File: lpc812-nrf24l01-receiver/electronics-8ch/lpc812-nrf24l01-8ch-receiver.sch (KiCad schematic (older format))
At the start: 23 parts, among them J1 CH1, J2 CH2/Rx, J3 CH3, J4 CH4, J5 CH5/Tx, J6 CH6, J7 CH7, J8 CH8, SW1 BIND/ISP, U1 MCP1703A-3302_SOT23, U2 LPC812M101JDH20, U3 NRF24L01_E01_ML01, Y1 12MHz

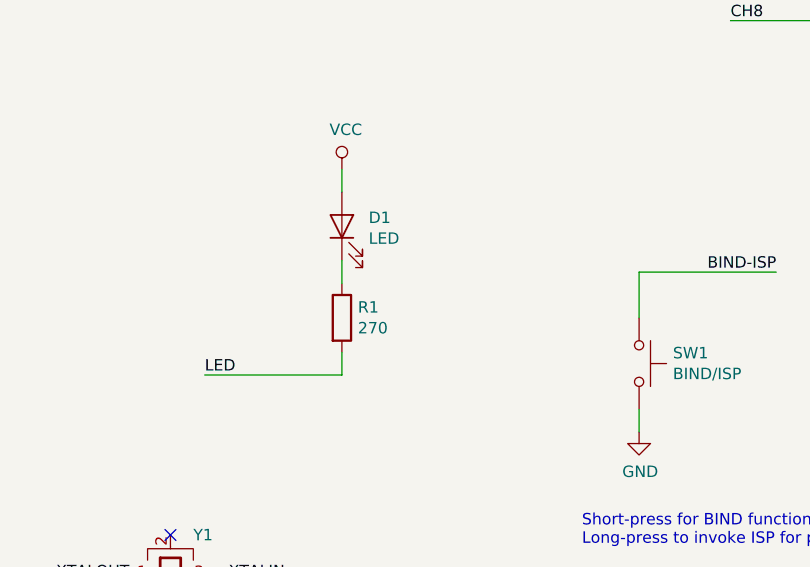
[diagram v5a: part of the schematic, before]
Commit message: Change LED resistor value
Update library to latest version of KiCad
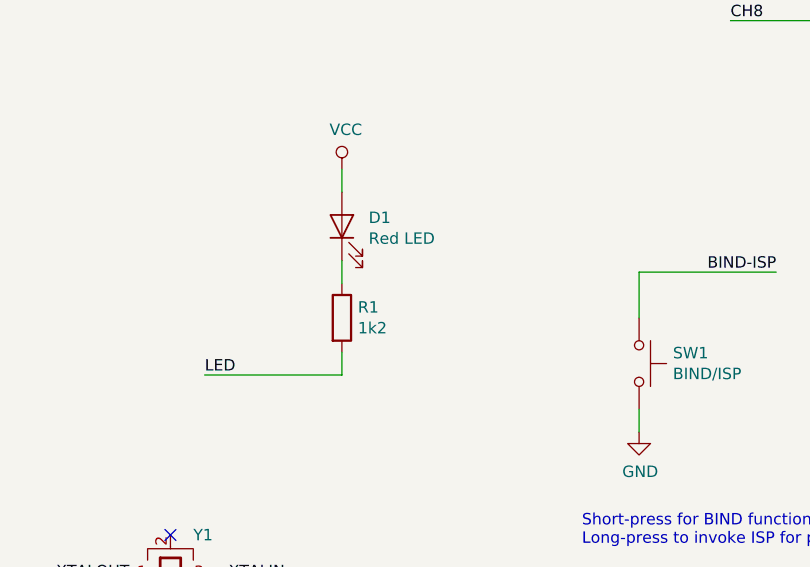
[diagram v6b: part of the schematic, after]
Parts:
- D1: value LED -> Red LED
- R1: value 270 -> 1k2
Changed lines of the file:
@@
 P 6350 4700
 F 0 "D1" V 6388 4583 50  0000 R CNN
-F 1 "LED" V 6297 4583 50  0000 R CNN
+F 1 "Red LED" V 6297 4583 50  0000 R CNN
 F 2 "LED_SMD:LED_0603_1608Metric_Pad1.05x0.95mm_HandSolder" H 6350 4700 50  0001 C CNN
 F 3 "~" H 6350 4700 50  0001 C CNN
@@
 P 6350 5100
 F 0 "R1" H 6420 5146 50  0000 L CNN
-F 1 "270" H 6420 5055 50  0000 L CNN
+F 1 "1k2" H 6420 5055 50  0000 L CNN
 F 2 "Resistor_SMD:R_0603_1608Metric_Pad1.05x0.95mm_HandSolder" V 6280 5100 50  0001 C CNN
 F 3 "~" H 6350 5100 50  0001 C CNN
